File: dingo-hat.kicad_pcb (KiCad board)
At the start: 2 copper layers, 65 x 56 mm, 84 parts, among them J1 LiPo-Power, J10 PJ-038AH, J11 Bypass-Power, J12 Chassis-Out, J13 i2c_display, J14 NEOPIXEL, J15 MPU-9250, J16 i2c_display_1, J2 Raspberry_Pi_2_3, J24 M2.5_Mount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

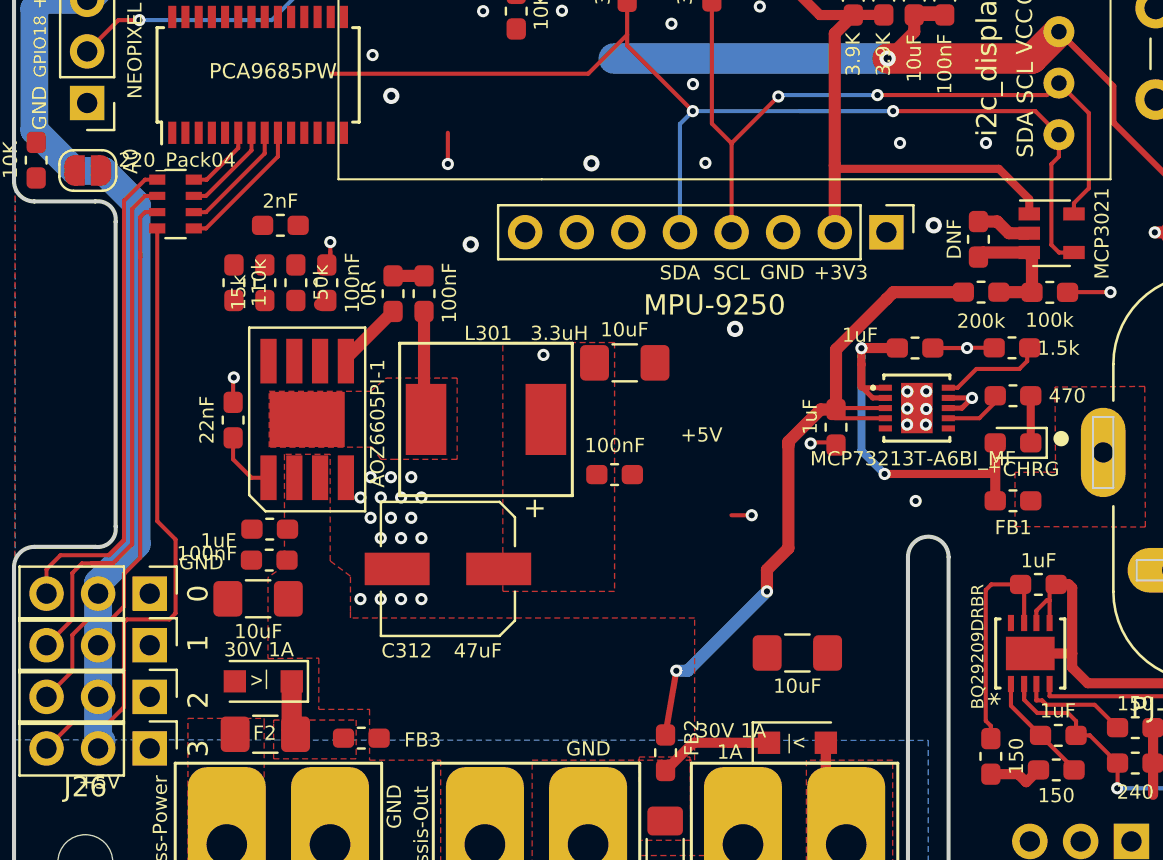
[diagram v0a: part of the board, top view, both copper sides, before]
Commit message: Flipping IMU to back of board.
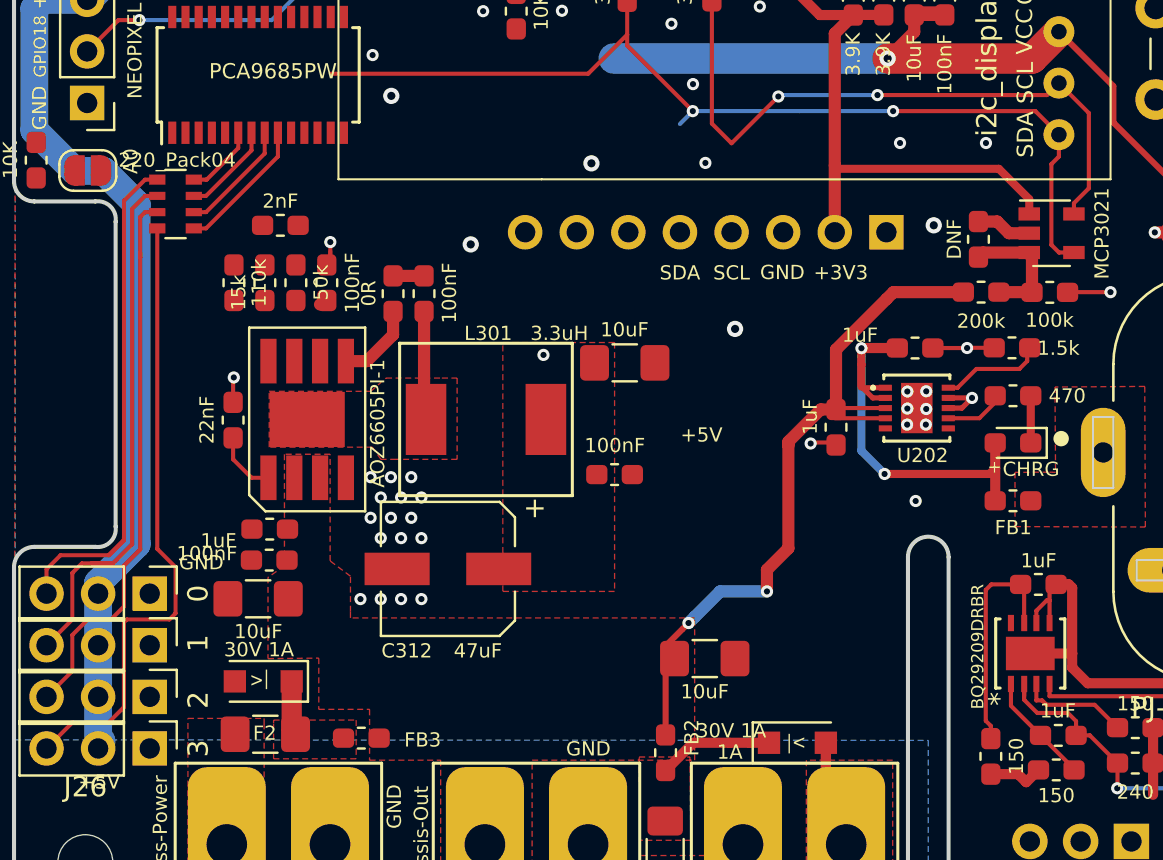
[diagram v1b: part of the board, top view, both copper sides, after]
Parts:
- J15: moved to B.Cu
- moved C302 4.57 mm to (134.0, 86.0)
- turned J15 to 90 degrees
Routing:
- net /SDA_3.3: track 58.6 -> 53.3 mm
- net /SCL_3.3: track 50.3 -> 45.9 mm
- net GND: track 30.0 -> 27.5 mm, vias 52 -> 49
- net /BatterySupply: track 35.8 -> 37.0 mm
- net Net-(R301-Pad2): track 3.41 -> 4.01 mm

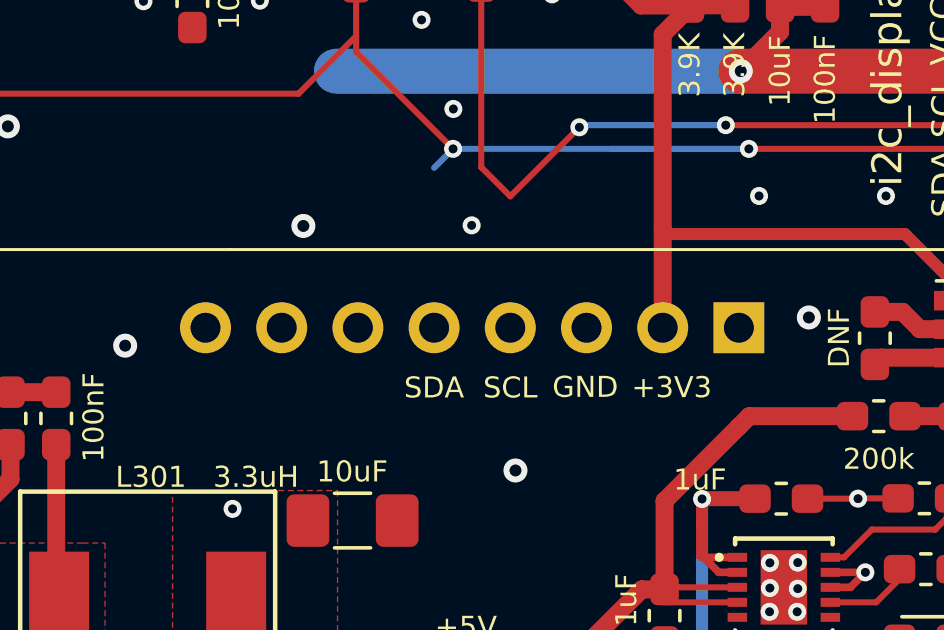
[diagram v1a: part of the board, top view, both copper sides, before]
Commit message: IMU now properly flipped.
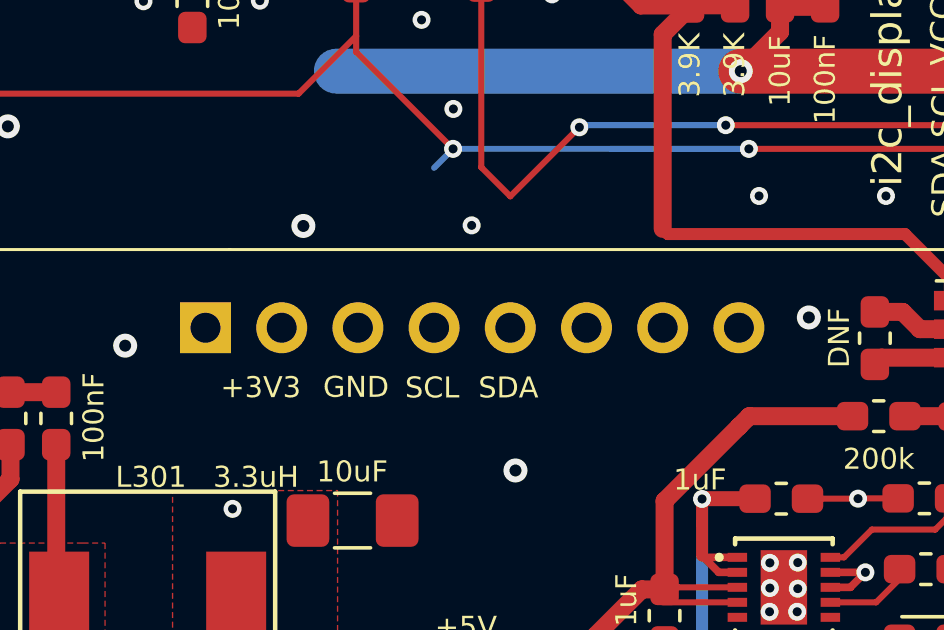
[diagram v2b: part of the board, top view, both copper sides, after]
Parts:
- moved J15 17.8 mm to (125.2, 65.0), turned to 270 degrees
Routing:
- net +3V3: track 63.8 -> 60.5 mm, vias 0 -> 1
- net GND: vias 49 -> 48
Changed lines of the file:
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@@
     (thickness 1.6)
     (drawings 95)
-    (tracks 399)
+    (tracks 398)
     (zones 0)
     (modules 84)
@@
   )
   (module Connector_PinHeader_2.54mm:PinHeader_1x08_P2.54mm_Vertical (layer B.Cu)
-    (at 142.938 65.016 90)
+    (at 125.158 65.016 270)
     (descr "Through hole straight pin header, 1x08, 2.54mm pitch, single row")
     (tags "Through hole pin header THT 1x08 2.54mm single row")
@@
       (effects (font (size 1 1) (thickness 0.15)) (justify mirror))
     )
-    (pad 1 thru_hole rect (at 0 0 90) (size 1.7 1.7) (drill 1) (layers *.Cu *.Mask)
+    (pad 1 thru_hole rect (at 0 0 270) (size 1.7 1.7) (drill 1) (layers *.Cu *.Mask)
       (net 60 "Net-(J15-Pad1)"))
-    (pad 2 thru_hole oval (at 0 -2.54 90) (size 1.7 1.7) (drill 1) (layers *.Cu *.Mask)
+    (pad 2 thru_hole oval (at 0 -2.54 270) (size 1.7 1.7) (drill 1) (layers *.Cu *.Mask)
       (net 23 +3V3))
-    (pad 3 thru_hole oval (at 0 -5.08 90) (size 1.7 1.7) (drill 1) (layers *.Cu *.Mask)
+    (pad 3 thru_hole oval (at 0 -5.08 270) (size 1.7 1.7) (drill 1) (layers *.Cu *.Mask)
       (net 1 GND))
-    (pad 4 thru_hole oval (at 0 -7.62 90) (size 1.7 1.7) (drill 1) (layers *.Cu *.Mask)
+    (pad 4 thru_hole oval (at 0 -7.62 270) (size 1.7 1.7) (drill 1) (layers *.Cu *.Mask)
       (net 21 /SCL_3.3))
-    (pad 5 thru_hole oval (at 0 -10.16 90) (size 1.7 1.7) (drill 1) (layers *.Cu *.Mask)
+    (pad 5 thru_hole oval (at 0 -10.16 270) (size 1.7 1.7) (drill 1) (layers *.Cu *.Mask)
       (net 22 /SDA_3.3))
-    (pad 6 thru_hole oval (at 0 -12.7 90) (size 1.7 1.7) (drill 1) (layers *.Cu *.Mask)
+    (pad 6 thru_hole oval (at 0 -12.7 270) (size 1.7 1.7) (drill 1) (layers *.Cu *.Mask)
       (net 61 /SD0\SA0))
-    (pad 7 thru_hole oval (at 0 -15.24 90) (size 1.7 1.7) (drill 1) (layers *.Cu *.Mask)
+    (pad 7 thru_hole oval (at 0 -15.24 270) (size 1.7 1.7) (drill 1) (layers *.Cu *.Mask)
       (net 51 /NCS))
-    (pad 8 thru_hole oval (at 0 -17.78 90) (size 1.7 1.7) (drill 1) (layers *.Cu *.Mask)
+    (pad 8 thru_hole oval (at 0 -17.78 270) (size 1.7 1.7) (drill 1) (layers *.Cu *.Mask)
       (net 62 /CSB))
   )
@@
     (effects (font (size 0.7 0.7) (thickness 0.175)) (justify mirror))
   )
-  (gr_text +3V3 (at 140.698 67.006) (layer B.SilkS)
+  (gr_text +3V3 (at 127.635 67.006) (layer B.SilkS)
     (effects (font (size 0.7 0.7) (thickness 0.175)) (justify mirror))
   )
-  (gr_text SDA (at 132.778 67.016) (layer B.SilkS)
+  (gr_text SDA (at 135.255 67.016) (layer B.SilkS)
     (effects (font (size 0.7 0.7) (thickness 0.175)) (justify mirror))
   )
-  (gr_text SCL (at 135.318 67.016) (layer B.SilkS)
+  (gr_text SCL (at 132.715 67.016) (layer B.SilkS)
     (effects (font (size 0.7 0.7) (thickness 0.175)) (justify mirror))
   )
-  (gr_text SDA (at 132.778 67.016) (layer F.SilkS)
+  (gr_text SDA (at 135.255 67.016) (layer F.SilkS)
     (effects (font (size 0.7 0.7) (thickness 0.175)))
   )
-  (gr_text SCL (at 135.318 67.016) (layer F.SilkS)
+  (gr_text SCL (at 132.715 67.016) (layer F.SilkS)
     (effects (font (size 0.7 0.7) (thickness 0.175)))
   )
-  (gr_text +3V3 (at 140.698 67.006) (layer F.SilkS)
+  (gr_text +3V3 (at 127 67.006) (layer F.SilkS)
     (effects (font (size 0.7 0.7) (thickness 0.175)))
   )
-  (gr_text GND (at 137.814678 67.003858) (layer B.SilkS)
+  (gr_text GND (at 130.175 67.003858) (layer B.SilkS)
     (effects (font (size 0.7 0.7) (thickness 0.175)) (justify mirror))
   )
-  (gr_text GND (at 137.818 66.996) (layer F.SilkS)
+  (gr_text GND (at 130.175 66.996) (layer F.SilkS)
     (effects (font (size 0.7 0.7) (thickness 0.175)))
   )
@@
   (via (at 106.19 97.854) (size 0.6) (drill 0.3) (layers F.Cu B.Cu) (net 1))
   (via (at 118.57 58.304) (size 0.8) (drill 0.4) (layers F.Cu B.Cu) (net 1))
-  (via (at 145.27 64.674) (size 0.8) (drill 0.4) (layers F.Cu B.Cu) (net 1))
+  (via (at 145.27 64.674) (size 0.8) (drill 0.4) (layers F.Cu B.Cu) (net 23))
   (via (at 122.48 65.614) (size 0.8) (drill 0.4) (layers F.Cu B.Cu) (net 1))
   (via (at 128.42 61.624) (size 0.8) (drill 0.4) (layers F.Cu B.Cu) (net 1))
@@
   (segment (start 149.97 64.114) (end 149.97 63.389) (width 0.4) (layer F.Cu) (net 23))
   (segment (start 140.398 55.237) (end 140.398 61.722) (width 0.6) (layer F.Cu) (net 23))
-  (segment (start 140.398 61.722) (end 140.398 65.016) (width 0.6) (layer F.Cu) (net 23))
   (segment (start 160.681 65.044) (end 160.701 65.064) (width 0.2032) (layer F.Cu) (net 24))
   (segment (start 158.636 65.044) (end 160.681 65.044) (width 0.2032) (layer F.Cu) (net 24))

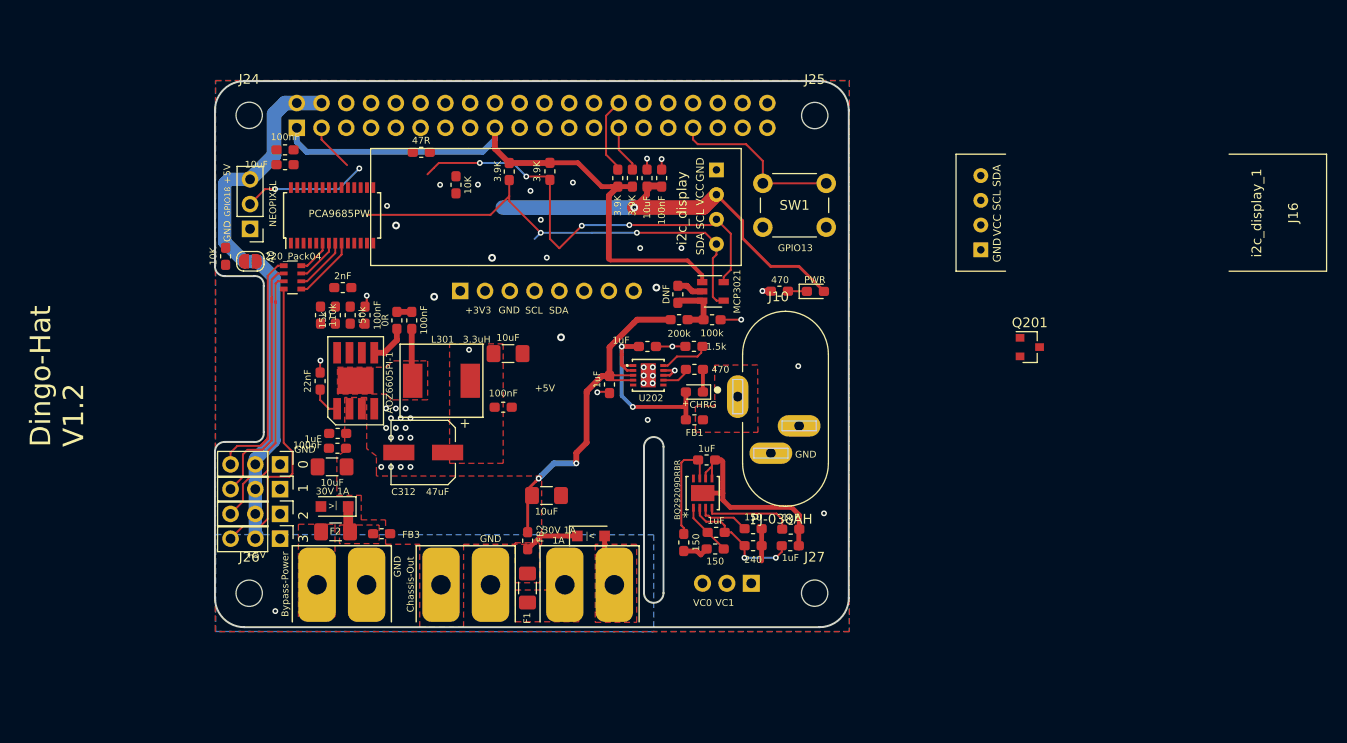
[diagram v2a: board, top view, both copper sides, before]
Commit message: Trying to add in the ultrasonics, other bits.
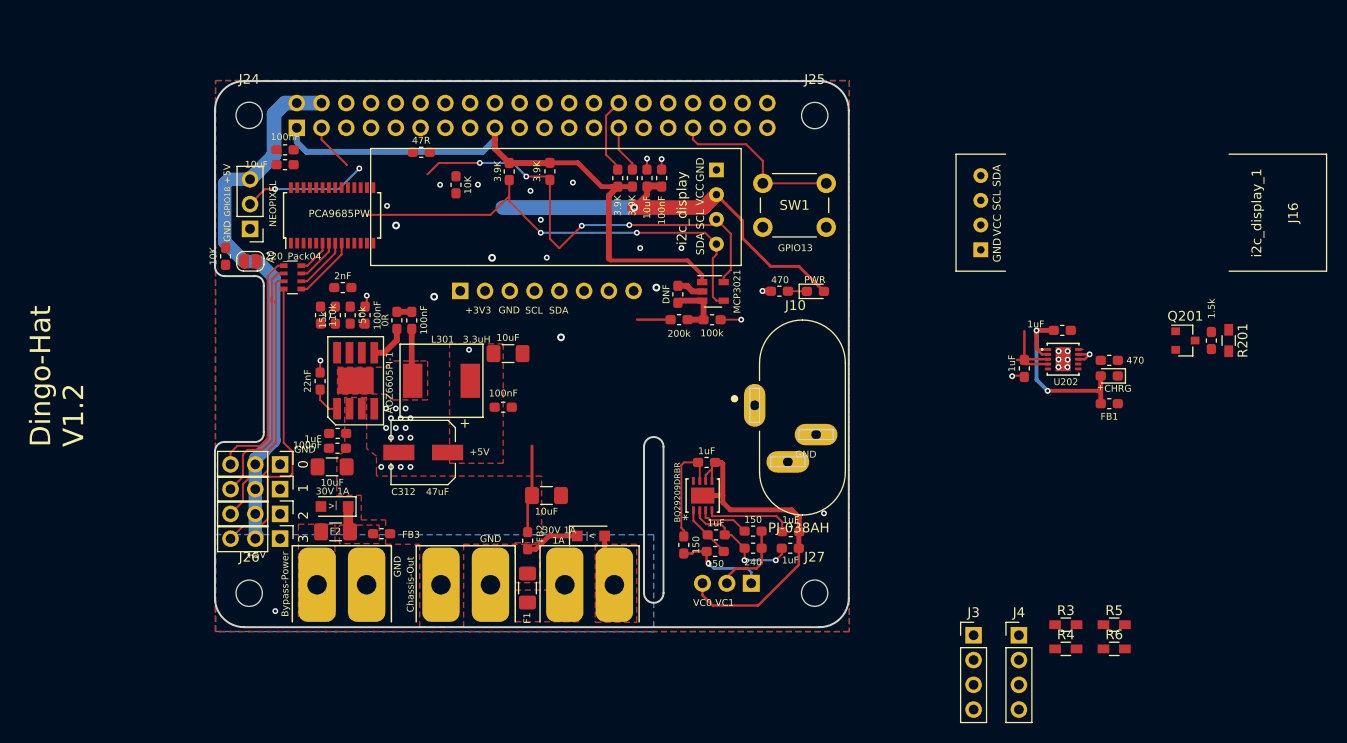
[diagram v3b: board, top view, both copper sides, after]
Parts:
- added J3: ULTRA_0, Pin_Headers:Pin_Header_Straight_1x04_Pitch2.54mm, F.Cu at (177.8, 100.3)
- added J4: ULTRA_1, Pin_Headers:Pin_Header_Straight_1x04_Pitch2.54mm, F.Cu at (182.4, 100.3)
- added R201: 10K, Resistors_SMD:R_0603_HandSoldering, F.Cu at (204.0, 70.1)
- added R3: 330, Resistors_SMD:R_0603_HandSoldering, F.Cu at (187.3, 99.2)
- added R4: 470, Resistors_SMD:R_0603_HandSoldering, F.Cu at (187.3, 101.7)
- added R5: 330, Resistors_SMD:R_0603_HandSoldering, F.Cu at (192.2, 99.2)
- added R6: 470, Resistors_SMD:R_0603_HandSoldering, F.Cu at (192.2, 101.7)
- moved R204 53.1 mm to (202.2, 70.1), turned to 270 degrees
- moved C202 42.6 mm to (186.9, 69.1)
- moved D201 42.6 mm to (191.7, 73.7)
- moved FB1 42.6 mm to (191.7, 76.6)
- moved C204 42.6 mm to (183.0, 73.0)
- moved U202 42.6 mm to (187.0, 72.0)
- moved R202 42.6 mm to (191.7, 72.1)
- moved Q201 16.0 mm to (199.5, 70.1)
- moved J10 1.96 mm to (160.2, 78.0)
- moved C205 0.25 mm to (151.4, 90.0)
- moved C208 0.25 mm to (150.4, 82.6)
- moved R208 0.25 mm to (148.1, 91.1)
- moved U203 0.25 mm to (150.0, 86.0)
- moved C206 0.25 mm to (159.0, 91.4)
- moved C207 0.25 mm to (159.1, 89.7)
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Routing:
- net /BatterySupply: track 37.0 -> 21.9 mm, vias 2 -> 0
- net /VC0: track 26.9 -> 41.9 mm
- net /VC2: track 2.76 -> 9.63 mm, vias 0 -> 1
- net Net-(R204-Pad1): track 5.23 -> 0.00 mm
- net /VC1: track 3.30 -> 8.07 mm
- net Net-(R202-Pad2): track 3.16 -> 0.00 mm
- net GND: track 27.5 -> 24.8 mm, vias 48 -> 45
- net Net-(D201-Pad1): track 2.32 -> 0.00 mm
- net /SDA_3.3: track 53.3 -> 52.4 mm
- net Net-(Q201-Pad2): track 0.00 -> 0.61 mm
- removed copper zone on F.Cu, net Net-(FB1-Pad2)

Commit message: Maybe just re-layout the whole thing.
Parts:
- moved J16 61.5 mm to (134.6, 68.5), turned to 270 degrees
- moved U1 19.7 mm to (134.9, 76.3), turned to 90 degrees
- moved C1 19.0 mm to (135.2, 79.9), turned to 180 degrees
- moved R10 17.3 mm to (118.8, 39.8)
- moved R11 17.3 mm to (122.9, 39.8)
- moved R13 15.6 mm to (137.8, 76.3), turned to 270 degrees
- moved R12 15.3 mm to (137.8, 79.7), turned to 90 degrees
- moved R2 13.9 mm to (113.5, 39.1)
- moved Q201 7.73 mm to (191.9, 68.8)
- moved R204 7.73 mm to (194.6, 68.8)
- moved R201 7.73 mm to (196.3, 68.8)
- moved R7 4.90 mm to (119.9, 53.3)
- moved SW1 1.91 mm to (156.2, 52.1)
- moved C311 1.50 mm to (128.9, 70.5), turned to 90 degrees
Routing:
- net /SDA_3.3: track 52.4 -> 6.18 mm, vias 2 -> 0
- net /SCL_3.3: track 45.9 -> 15.5 mm, vias 4 -> 0
- net +3V3: track 60.5 -> 33.8 mm, vias 1 -> 0
- net /BatterySupply: track 21.9 -> 18.5 mm
- net /GPIO13: track 18.1 -> 15.2 mm
- net GND: vias 45 -> 41
